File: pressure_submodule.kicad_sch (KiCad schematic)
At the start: 17 parts, among them IC12 PINA350ABSIDDFR, J14 Conn_01x04, Q12 BSZ0902NSATMA1

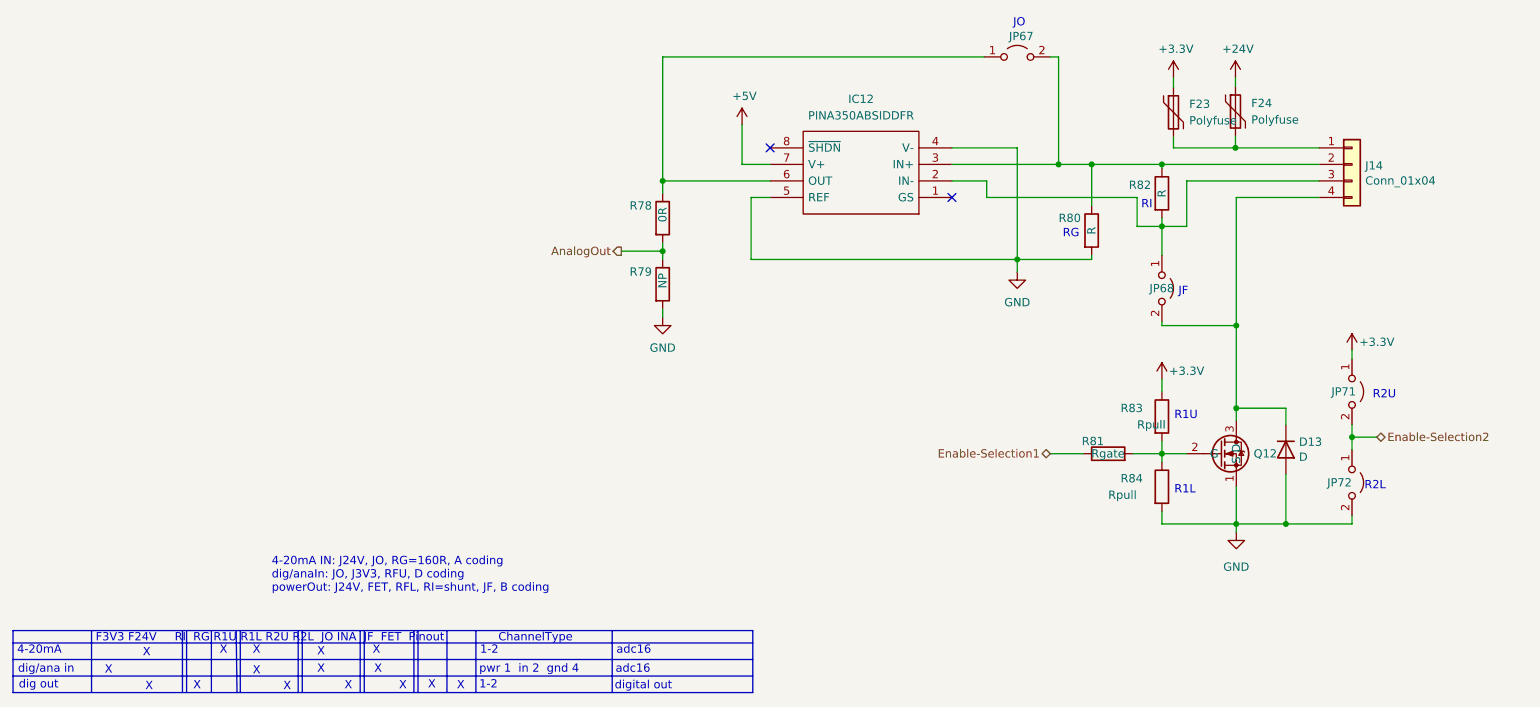
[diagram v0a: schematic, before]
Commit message: Added JP for GS + Cap @STM Pin 1
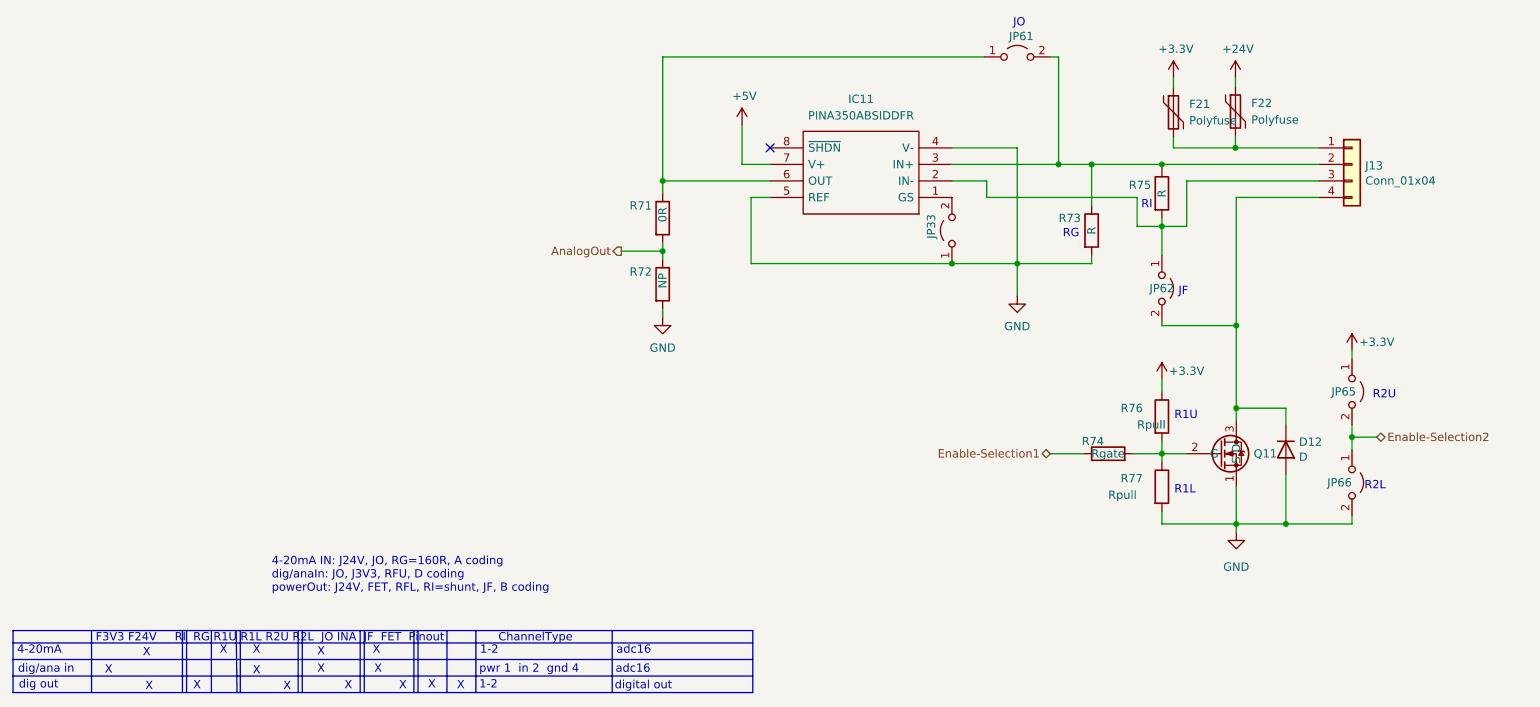
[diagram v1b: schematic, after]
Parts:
- added JP33: Jumper_2_Open, Jumper:SolderJumper-2_P1.3mm_Open_TrianglePad1.0x1.5mm, symbol Jumper:Jumper_2_Open
- renumbered D13 to D12, F23 to F21, F24 to F22, IC12 to IC11, J14 to J13, JP67 to JP61, JP68 to JP62, JP71 to JP65, JP72 to JP66, Q12 to Q11, R78 to R71, R79 to R72, R80 to R73, R81 to R74, R82 to R75, R83 to R76, R84 to R77
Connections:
- net GND: now also JP33.1 (A)
- net at IC11.1 (GS): now also JP33.2 (B)
- no-connect marks 2 -> 1

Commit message: Changed 5V Plane to 3.3V Changed INA350 Supply to 3.3V Minor tweaks
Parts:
- IC1: renamed from IC11; footprint SOT65P280X110-8N -> KiCad:SOT65P280X110-8N
- renumbered D12 to D2, F21 to F1, F22 to F2, J13 to J3, JP61 to JP1, JP62 to JP2, JP33 to JP3, JP65 to JP5, JP66 to JP6, Q11 to Q1, R71 to R1, R72 to R2, R73 to R3, R74 to R4, R75 to R5, R76 to R6, R77 to R7
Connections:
- net +5V is gone; now on net +3V3: IC1.7 (V+)

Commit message: Fixed Lib Mess
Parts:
- IC1: footprint KiCad:SOT65P280X110-8N -> SOT65P280X110-8N; symbol PINA350ABSIDDFR:PINA350ABSIDDFR -> TXV_Library_Symbols:PINA350ABSIDDFR
- Q1: symbol IOB-rescue:BSZ0902NSATMA1-TXV_Library_Symbols -> TXV_Library_Symbols:BSZ0902NSATMA1
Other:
- moved on the sheet: JP3
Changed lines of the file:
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@@
 (kicad_sch (version 20211123) (generator eeschema)
   (paper "A4")
-  (junction (at 179.832 104.521) (diameter 0) (color 0 0 0 0)
-  )
   (junction (at 212.09 89.281) (diameter 0) (color 0 0 0 0)
   )
@@
   )
   (junction (at 201.295 89.281) (diameter 0) (color 0 0 0 0)
+  )
+  (junction (at 181.864 104.521) (diameter 0) (color 0 0 0 0)
   )
   (junction (at 212.09 98.806) (diameter 0) (color 0 0 0 0)
@@
     (stroke (width 0) (type default) (color 0 0 0 0))
   )
+  (wire (pts (xy 181.864 94.361) (xy 179.832 94.361))
+    (stroke (width 0) (type default) (color 0 0 0 0))
+  )
   (polyline (pts (xy 35.56 165.354) (xy 149.225 165.354))
     (stroke (width 0) (type default) (color 0 0 0 0))
@@
     (stroke (width 0) (type default) (color 0 0 0 0))
   )
-  (wire (pts (xy 179.832 104.521) (xy 189.865 104.521))
-    (stroke (width 0) (type default) (color 0 0 0 0))
-  )
   (polyline (pts (xy 79.375 160.909) (xy 79.375 170.434))
     (stroke (width 0) (type default) (color 0 0 0 0))
@@
     (stroke (width 0) (type default) (color 0 0 0 0))
   )
-  (wire (pts (xy 179.832 104.521) (xy 148.971 104.521))
-    (stroke (width 0) (type default) (color 0 0 0 0))
-  )
   (polyline (pts (xy 62.23 160.909) (xy 62.23 170.434))
     (stroke (width 0) (type default) (color 0 0 0 0))
@@
     (stroke (width 0) (type default) (color 0 0 0 0))
   )
+  (wire (pts (xy 148.971 104.521) (xy 181.864 104.521))
+    (stroke (width 0) (type default) (color 0 0 0 0))
+  )
   (polyline (pts (xy 47.625 160.909) (xy 47.625 170.434))
     (stroke (width 0) (type default) (color 0 0 0 0))
@@
   )
   (polyline (pts (xy 88.9 160.909) (xy 88.9 170.434))
+    (stroke (width 0) (type default) (color 0 0 0 0))
+  )
+  (wire (pts (xy 181.864 104.521) (xy 189.865 104.521))
     (stroke (width 0) (type default) (color 0 0 0 0))
   )
@@
     (pin "2")
   )
-  (symbol (lib_id "Jumper:Jumper_2_Open") (at 179.832 99.441 90) (unit 1)
-    (in_bom yes) (on_board yes)
-    (property "Reference" "JP3" (id 0) (at 176.657 100.711 0)
-      (effects (font (size 1.27 1.27)) (justify left))
-    )
-    (property "Value" "Jumper_2_Open" (id 1) (at 177.3428 98.298 90)
-      (effects (font (size 1.27 1.27)) (justify left) hide)
-    )
-    (property "Footprint" "Jumper:SolderJumper-2_P1.3mm_Open_TrianglePad1.0x1.5mm" (id 2) (at 179.832 99.441 0)
-      (effects (font (size 1.27 1.27)) hide)
-    )
-    (property "Datasheet" "~" (id 3) (at 179.832 99.441 0)
+  (symbol (lib_id "Jumper:Jumper_2_Open") (at 181.864 99.441 90) (unit 1)
+    (in_bom yes) (on_board yes)
+    (property "Reference" "JP3" (id 0) (at 178.689 100.711 0)
+      (effects (font (size 1.27 1.27)) (justify left))
+    )
+    (property "Value" "Jumper_2_Open" (id 1) (at 179.3748 98.298 90)
+      (effects (font (size 1.27 1.27)) (justify left) hide)
+    )
+    (property "Footprint" "Jumper:SolderJumper-2_P1.3mm_Open_TrianglePad1.0x1.5mm" (id 2) (at 181.864 99.441 0)
+      (effects (font (size 1.27 1.27)) hide)
+    )
+    (property "Datasheet" "~" (id 3) (at 181.864 99.441 0)
       (effects (font (size 1.27 1.27)) hide)
     )
@@
     (pin "2")
   )
-  (symbol (lib_id "PINA350ABSIDDFR:PINA350ABSIDDFR") (at 179.832 94.361 180) (unit 1)
+  (symbol (lib_id "TXV_Library_Symbols:PINA350ABSIDDFR") (at 179.832 94.361 180) (unit 1)
     (in_bom yes) (on_board yes) (fields_autoplaced)
     (property "Reference" "IC1" (id 0) (at 165.862 79.248 0))
     (property "Value" "PINA350ABSIDDFR" (id 1) (at 165.862 81.788 0))
-    (property "Footprint" "KiCad:SOT65P280X110-8N" (id 2) (at 155.702 96.901 0)
+    (property "Footprint" "SOT65P280X110-8N" (id 2) (at 155.702 96.901 0)
       (effects (font (size 1.27 1.27)) (justify left) hide)
     )
@@
     (pin "2")
   )
-  (symbol (lib_id "IOB-rescue:BSZ0902NSATMA1-TXV_Library_Symbols") (at 222.25 133.731 0) (unit 1)
+  (symbol (lib_id "TXV_Library_Symbols:BSZ0902NSATMA1") (at 222.25 133.731 0) (unit 1)
     (in_bom yes) (on_board yes)
     (property "Reference" "Q1" (id 0) (at 226.187 133.731 0)
